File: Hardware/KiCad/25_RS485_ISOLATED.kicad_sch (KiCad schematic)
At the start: 0 parts

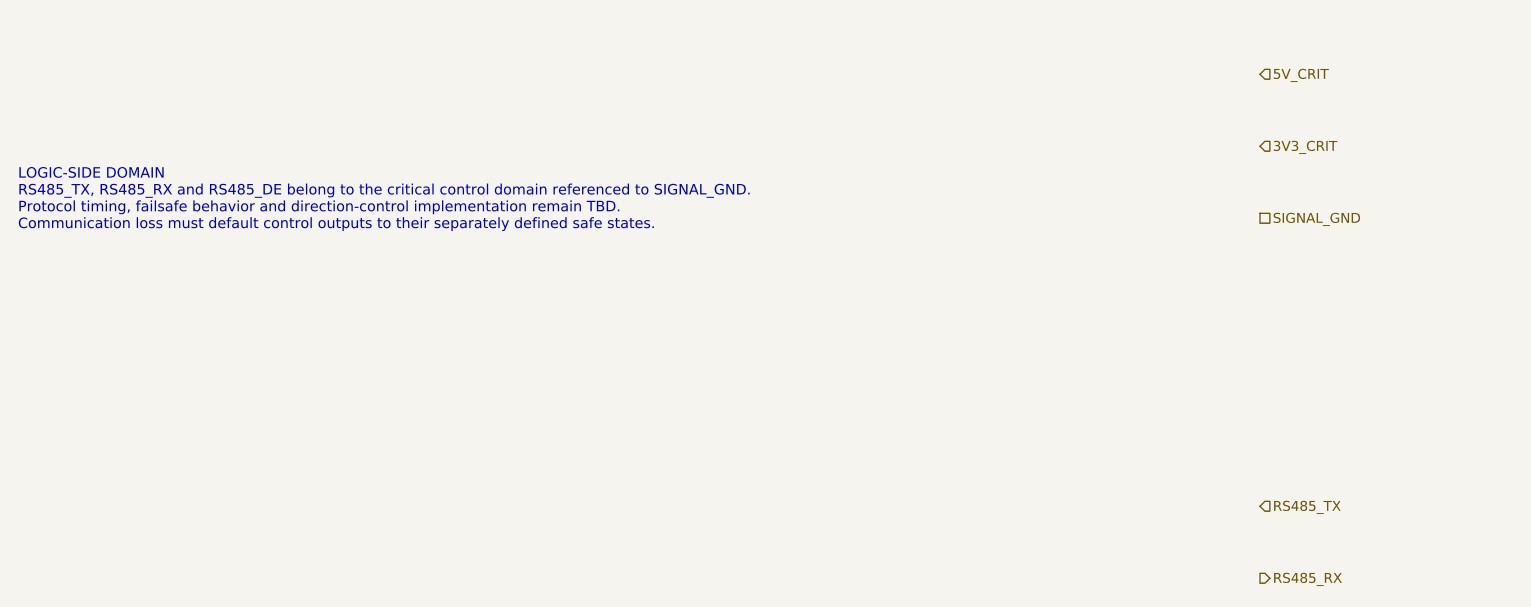
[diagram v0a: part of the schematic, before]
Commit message: hardware: align RS-485 logic group interface
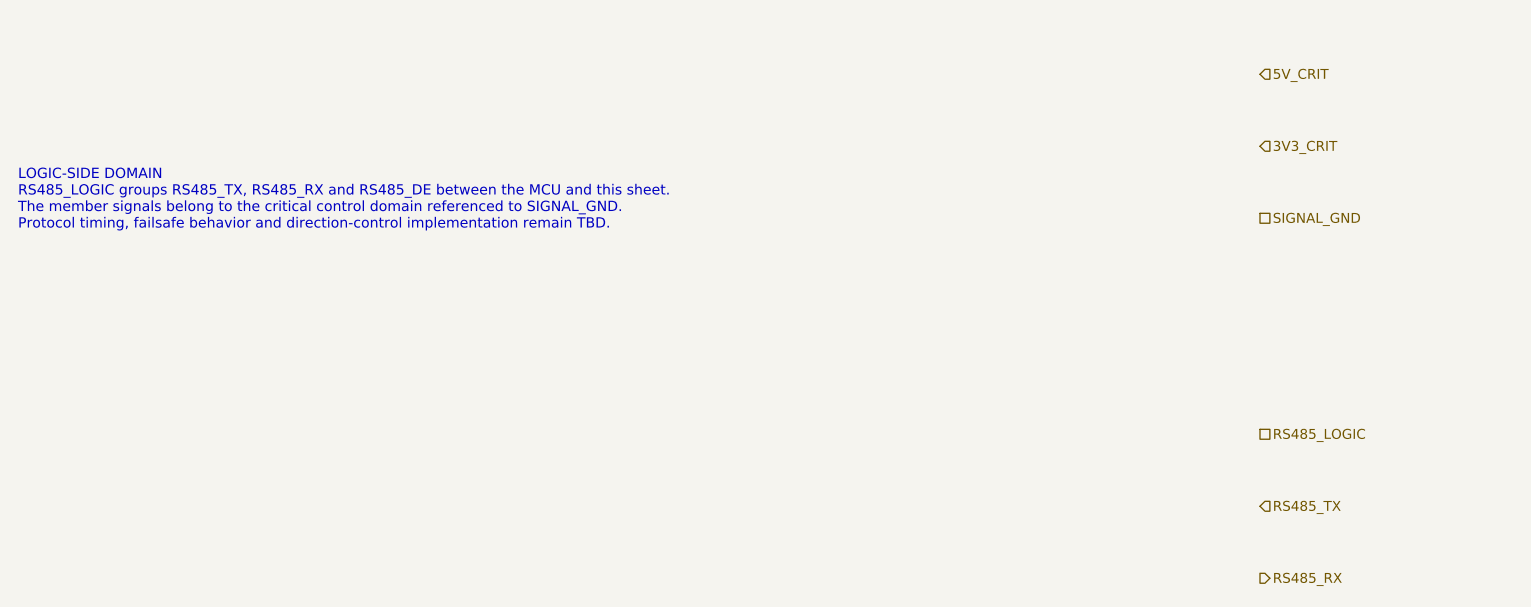
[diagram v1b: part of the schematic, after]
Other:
- note added: "LOGIC-SIDE DOMAIN RS485_LOGIC groups RS485_TX, RS485_RX and RS485_DE between the MCU and this sheet. The member signals belong to the critical control domain referenced to SIGNAL_GND. Protocol timing, failsafe behavior and direction-control implementation remain TBD."
- note removed: "LOGIC-SIDE DOMAIN RS485_TX, RS485_RX and RS485_DE belong to the critical control domain referenced to SIGNAL_GND. Protocol timing, failsafe behavior and direction-control implementation remain TBD. Communication loss must default control outputs to their separately defined safe states."
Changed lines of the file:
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@@
 		(title "25_RS485_ISOLATED - external half-duplex communication boundary")
 		(date "2026-07-15")
-		(rev "B0")
+		(rev "B1")
 		(company "Gonoboben/plataVM")
-		(comment 1 "Architecture Level A/B: isolated external RS-485 logic, barrier and cable-side domains")
+		(comment 1 "Interface consistency: RS485_LOGIC group and isolated external boundary")
 		(comment 2 "No transceiver, digital isolator, isolated supply, termination, TVS, connector or footprint selected")
 	)
@@
 		(uuid "ctrl-reserve-00000025-0000-4000-8000-000000000101")
 	)
-	(text "LOGIC-SIDE DOMAIN\nRS485_TX, RS485_RX and RS485_DE belong to the critical control domain referenced to SIGNAL_GND.\nProtocol timing, failsafe behavior and direction-control implementation remain TBD.\nCommunication loss must default control outputs to their separately defined safe states."
+	(text "LOGIC-SIDE DOMAIN\nRS485_LOGIC groups RS485_TX, RS485_RX and RS485_DE between the MCU and this sheet.\nThe member signals belong to the critical control domain referenced to SIGNAL_GND.\nProtocol timing, failsafe behavior and direction-control implementation remain TBD."
 		(exclude_from_sim no)
 		(at 12 72 0)
-		(effects (font (size 1.16 1.16)) (justify left))
+		(effects (font (size 1.14 1.14)) (justify left))
 		(uuid "ctrl-reserve-00000025-0000-4000-8000-000000000102")
 	)
@@
 	(hierarchical_label "3V3_CRIT" (shape input) (exclude_from_sim no) (at 150 66 0) (effects (font (size 1.1 1.1)) (justify left)) (uuid "ctrl-reserve-00000025-0000-4000-8000-000000000202"))
 	(hierarchical_label "SIGNAL_GND" (shape passive) (exclude_from_sim no) (at 150 74 0) (effects (font (size 1.1 1.1)) (justify left)) (uuid "ctrl-reserve-00000025-0000-4000-8000-000000000203"))
+	(hierarchical_label "RS485_LOGIC" (shape passive) (exclude_from_sim no) (at 150 98 0) (effects (font (size 1.1 1.1)) (justify left)) (uuid "ctrl-reserve-00000025-0000-4000-8000-000000000212"))
 	(hierarchical_label "RS485_TX" (shape input) (exclude_from_sim no) (at 150 106 0) (effects (font (size 1.1 1.1)) (justify left)) (uuid "ctrl-reserve-00000025-0000-4000-8000-000000000204"))
 	(hierarchical_label "RS485_RX" (shape output) (exclude_from_sim no) (at 150 114 0) (effects (font (size 1.1 1.1)) (justify left)) (uuid "ctrl-reserve-00000025-0000-4000-8000-000000000205"))
